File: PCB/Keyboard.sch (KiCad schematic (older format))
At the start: 25 parts, among them P1 USB_OTG, SW1 RST, U1 ATMEGA32U4-QFN44, X1 ABM10-16.000MHZ-D30-T3

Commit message: V1.1 prototype
Ordered as is from OSHPark and OSHStencils
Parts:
- F1: Mouser (none) -> 652-MFFSMF050X-2
- KB1: Mouser (none) -> 538-52437-2233
- SW1: Mouser (none) -> 688-SKRMAA
- U1: Mouser (none) -> 556-ATMEGA32U4RC-MU
- X1: Mouser (none) -> 815-ABM10-16-D30T3
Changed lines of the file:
@@
 F 3 "" H 10250 4600 60  0000 C CNN
 F 4 "2520146" H 10250 3800 60  0001 C CNN "Farnell"
+F 5 "538-52437-2233" H 10250 3800 60  0001 C CNN "Mouser"
 	1    10250 3800
 	1    0    0    -1
@@
 F 3 "" H 5650 5100 60  0000 C CNN
 F 4 "2425127" H 5650 3800 60  0001 C CNN "Farnell"
+F 5 "556-ATMEGA32U4RC-MU" H 5650 3800 60  0001 C CNN "Mouser"
 	1    5650 3800
 	1    0    0    -1
@@
 F 3 "" H 3900 3800 60  0000 C CNN
 F 4 "2467762" H 3900 3800 60  0001 C CNN "Farnell"
+F 5 "815-ABM10-16-D30T3" H 3900 3800 60  0001 C CNN "Mouser"
 	1    3900 3800
 	0    -1   -1   0
@@
 F 3 "" H 3650 2750 50  0000 C CNN
 F 4 "2376538" H 3650 2750 60  0001 C CNN "Farnell"
+F 5 "688-SKRMAA" H 3650 2750 60  0001 C CNN "Mouser"
 	1    3650 2750
 	1    0    0    -1
@@
 F 3 "" H 2100 4350 50  0000 C CNN
 F 4 "1717227" H 2100 4350 60  0001 C CNN "Farnell"
+F 5 "652-MFFSMF050X-2" H 2100 4350 60  0001 C CNN "Mouser"
 	1    2100 4350
 	1    0    0    -1

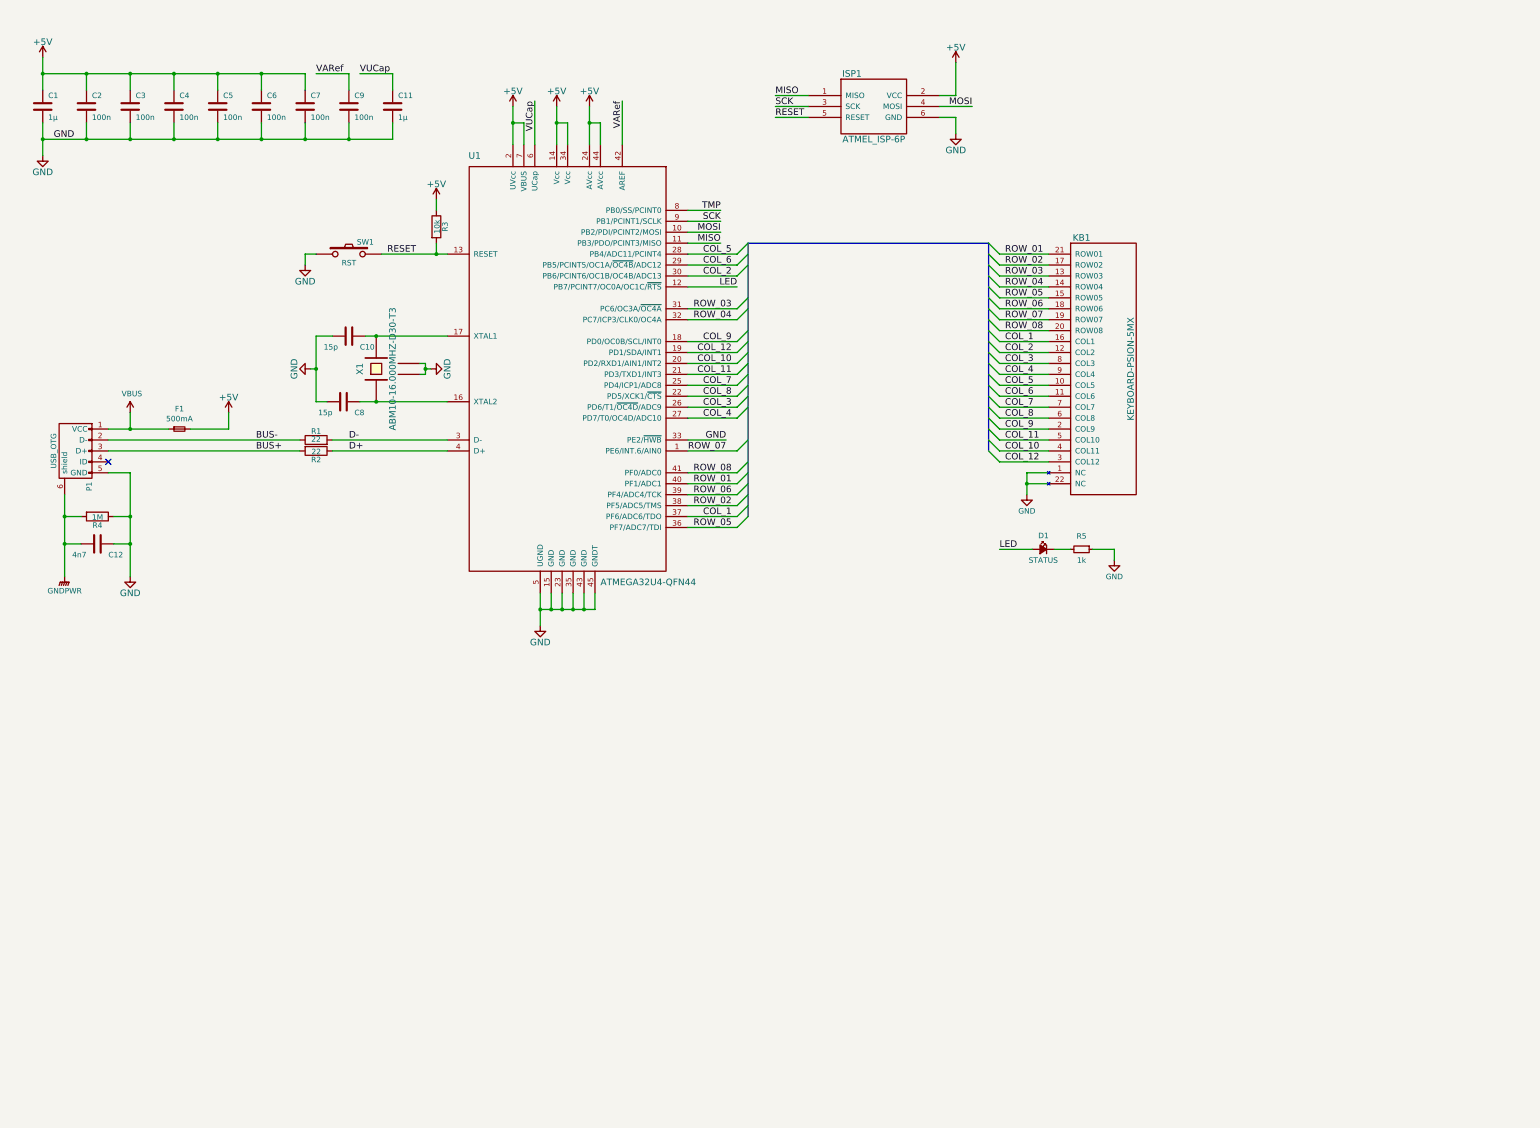
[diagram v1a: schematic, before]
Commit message: Added bootloader and script for flashing
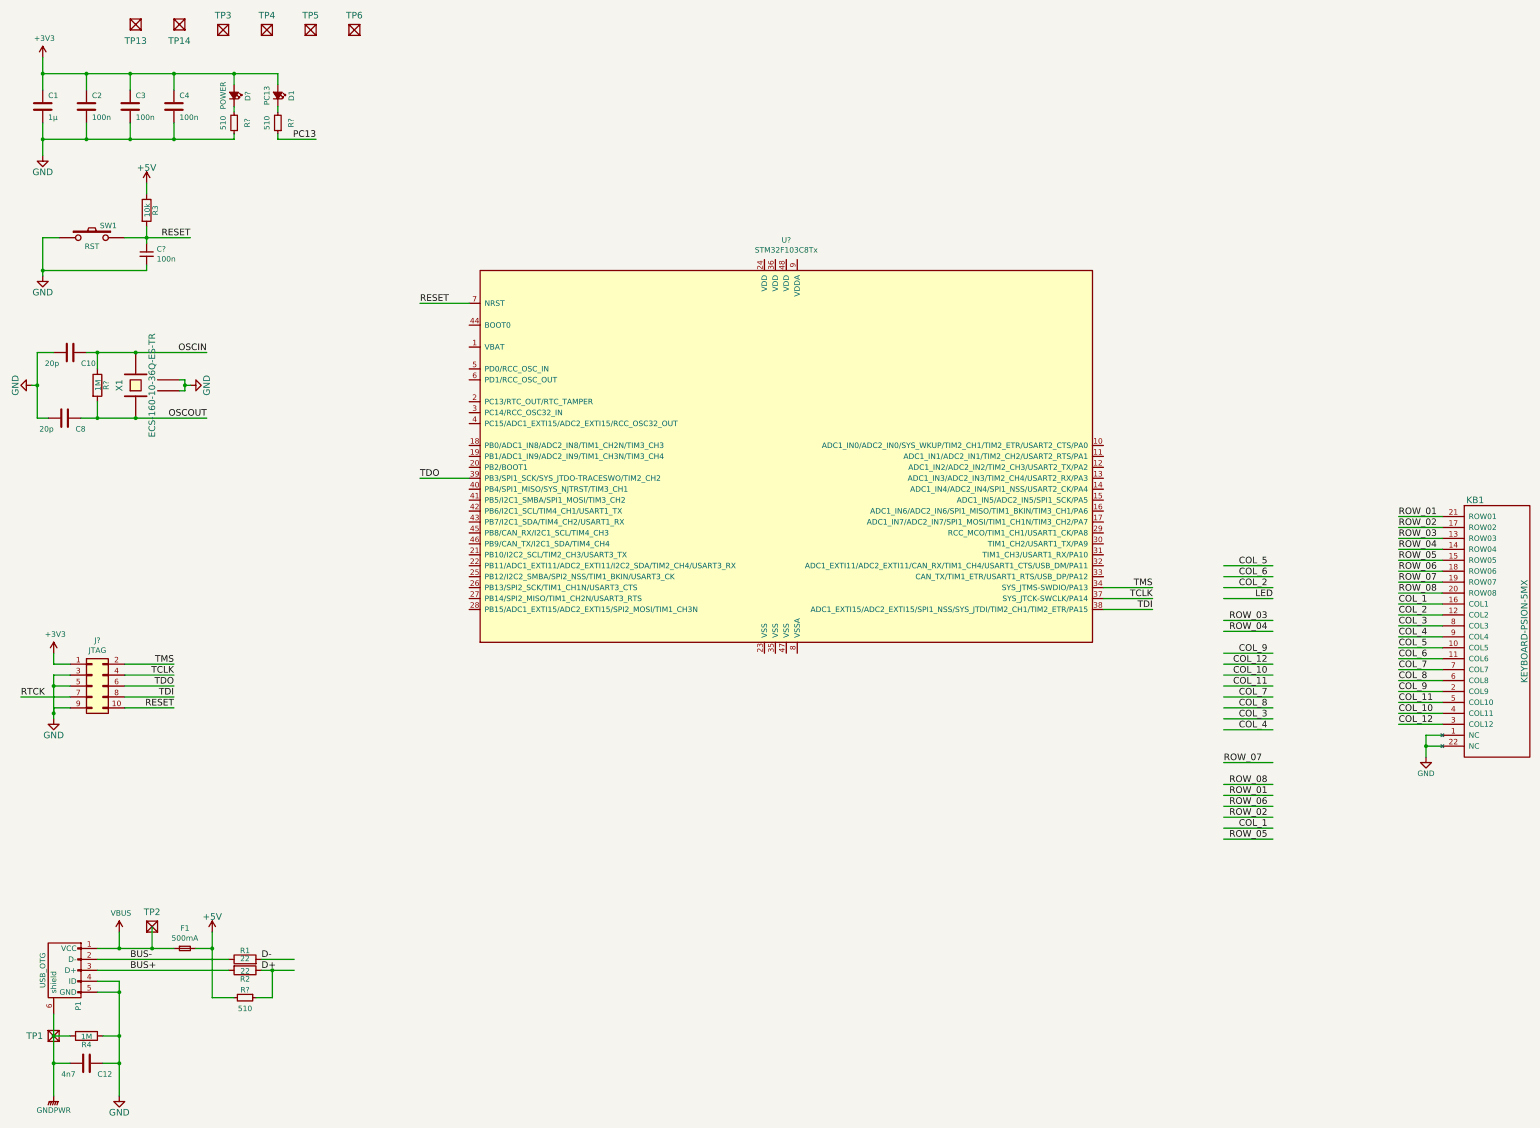
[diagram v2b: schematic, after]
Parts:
- removed C11: 1µ, SMD-DiscreteB:C-0402-1005, symbol C
- removed C5, C6, C7, C9: 100n, SMD-DiscreteB:C-0402-1005, symbol C
- removed ISP1: ATMEL_ISP-6P, SMD-Connectors:ISP-PADS_2mm54, symbol ATMEL_ISP-6P
- removed R5: 1k, SMD-DiscreteB:R-0402-1005, symbol R_Small
- removed U1: ATMEGA32U4-QFN44, SMD-QFN:VQFN-44_ATMEL, symbol ATMEGA32U4-QFN44
- added C?: 100n, symbol C_Small
- added D?: POWER, SMD-DiscreteB:LED-0402-1005, symbol Led_Small
- added J?: JTAG, symbol Conn_02x05_Odd_Even
- added R? (x3): 510, SMD-DiscreteB:R-0402-1005, symbol R_Small
- added R?: 1M, SMD-DiscreteB:R-0402-1005, symbol R
- added TP1, TP13, TP14, TP2, TP3, TP4, TP5, TP6: TESTPOINT, Vias_and_Pads:TestPoint_1.0mm, symbol TESTPOINT
- added U?: STM32F103C8Tx, Housings_QFP:LQFP-48_7x7mm_Pitch0.5mm, symbol STM32F103C8Tx
- C10, C8: value 15p -> 20p
- D1: value STATUS -> PC13
- KB1: Farnell 2520146 -> (none); Mouser 538-52437-2233 -> 649-SFV22R-1STE1HLF
- SW1: Farnell 2376538 -> (none); Mouser 688-SKRMAA -> 688-SKRMAB
- X1: value ABM10-16.000MHZ-D30-T3 -> ECS-160-10-36Q-ES-TR; Farnell 2467762 -> (none); Mouser 815-ABM10-16-D30T3 -> 520-160-10-36Q-EST
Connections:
- net labels added: +3V3, OSCIN, OSCOUT, PC13, RTCK, TCLK, TDI, TDO, TMS
- net labels removed: MISO, MOSI, SCK, TMP, VARef, VUCap
- wire segments 131 -> 148
- no-connect marks 1 -> 0
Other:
- moved on the sheet: C10, C12, C8, D1, F1, KB1, P1, R1, R2, R3, R4, SW1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
